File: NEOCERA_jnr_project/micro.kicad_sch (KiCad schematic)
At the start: 0 parts

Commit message: fully edited
edited :)
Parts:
- added D3: SM712_SOT23, Package_TO_SOT_SMD:SOT-23, symbol Diode:SM712_SOT23
- added D4: LED, LED_SMD:LED_0805_2012Metric, symbol Device:LED
- added FID1, FID2, FID3, FID4: Fiducial, Fiducial:Fiducial_1mm_Mask2mm, symbol Mechanical:Fiducial
- added R25: R, symbol Device:R
- added R26: 10k, symbol Device:R
- added TP1: TestPoint, TestPoint:TestPoint_THTPad_2.0x2.0mm_Drill1.0mm, symbol Connector:TestPoint
- added U12: PIC18F45K50_QFP, Package_QFP:TQFP-44_10x10mm_P0.8mm, symbol MCU_Microchip_PIC18:PIC18F45K50_QFP
- added Y1: ASV-xxxMHz, Oscillator:Oscillator_SMD_Abracon_ASV-4Pin_7.0x5.1mm, symbol Oscillator:ASV-xxxMHz
- added Y2: MAX7375AXR365, Package_TO_SOT_SMD:SOT-323_SC-70, symbol Oscillator:MAX7375AXR365
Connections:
- new net: R25.1, U12.3 (RD5/P1B/AN25)
- new net: U12.30 (OSC1/CLKI/RA7), Y1.3 (OUT)
- new net: R26.2, Y1.1 (EN)
- new net: D4.2 (A), R25.2
- new net +3.3V: R26.1, U12.28 (VDD), U12.8 (AN12/SRI/~{FLT0}/SDI/SDA/INT0/RB0), Y1.4 (Vdd)
- new net GND: D4.1 (K), TP1.1, U12.29 (VSS), U12.7 (VDD), Y1.2 (GND)

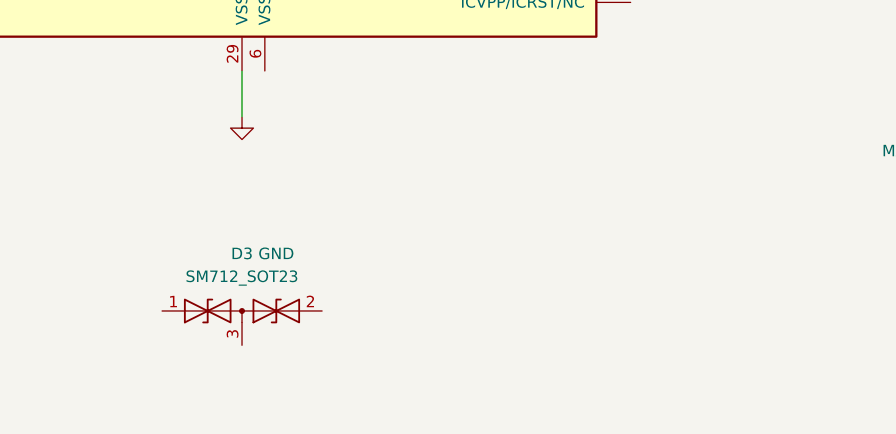
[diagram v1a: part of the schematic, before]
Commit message: update
- added symbol and programming header
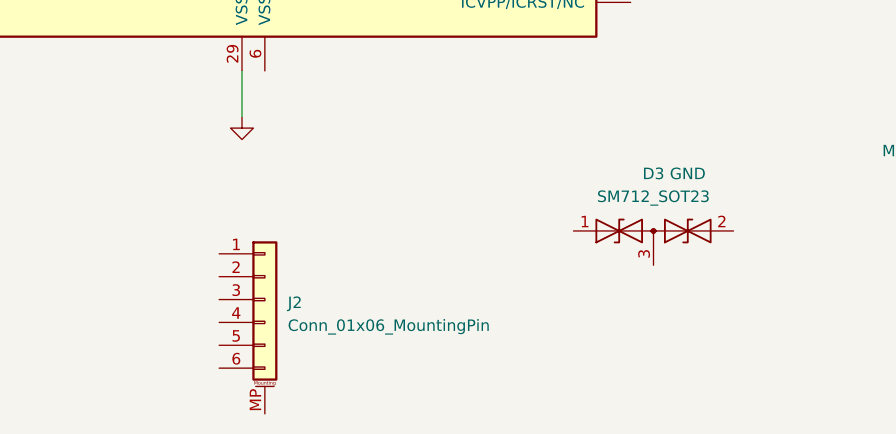
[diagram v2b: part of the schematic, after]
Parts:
- added J2: Conn_01x06_MountingPin, symbol Connector_Generic_MountingPin:Conn_01x06_MountingPin
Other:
- moved on the sheet: D3
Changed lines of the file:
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@@
+	)
+	(symbol
+		(lib_id "Connector_Generic_MountingPin:Conn_01x06_MountingPin")
+		(at 134.62 157.48 0)
+		(unit 1)
+		(exclude_from_sim no)
+		(in_bom yes)
+		(on_board yes)
+		(dnp no)
+		(fields_autoplaced yes)
+		(property "Reference" "J2"
+			(at 137.16 157.8355 0)
+			(effects
+				(font
+					(size 1.27 1.27)
+				)
+				(justify left)
+			)
+		)
+		(property "Value" "Conn_01x06_MountingPin"
+			(at 137.16 160.3755 0)
+			(effects
+				(font
+					(size 1.27 1.27)
+				)
+				(justify left)
+			)
+		)
+		(property "Footprint" ""
+			(at 134.62 157.48 0)
+			(effects
+				(font
+					(size 1.27 1.27)
+				)
+				(hide yes)
+			)
+		)
+		(property "Datasheet" "~"
+			(at 134.62 157.48 0)
+			(effects
+				(font
+					(size 1.27 1.27)
+				)
+				(hide yes)
+			)
+		)
+		(property "Description" "Generic connectable mounting pin connector, single row, 01x06, script generated (kicad-library-utils/schlib/autogen/connector/)"
+			(at 134.62 157.48 0)
+			(effects
+				(font
+					(size 1.27 1.27)
+				)
+				(hide yes)
+			)
+		)
+		(pin "5"
+		)
+		(pin "3"
+		)
+		(pin "4"
+		)
+		(pin "1"
+		)
+		(pin "6"
+		)
+		(pin "2"
+		)
+		(pin "MP"
+		)
+		(instances
+			(project ""
+				(path "/a8746ab6-0163-416c-99f9-0036ded73fc6/31b6b5cc-d086-44ba-8cec-c6130e1adfec"
+					(reference "J2")
+					(unit 1)
+				)
+			)
+		)
 	)
 	(symbol
@@
 		)
 		(property "Value" "GND"
-			(at 135.89 152.4 0)
+			(at 181.61 143.51 0)
 			(effects
 				(font
@@
 	(symbol
 		(lib_id "Diode:SM712_SOT23")
-		(at 132.08 158.75 0)
+		(at 177.8 149.86 0)
 		(unit 1)
 		(exclude_from_sim no)
@@
 		(fields_autoplaced yes)
 		(property "Reference" "D3"
-			(at 132.08 152.4 0)
+			(at 177.8 143.51 0)
 			(effects
 				(font
@@
 		)
 		(property "Value" "SM712_SOT23"
-			(at 132.08 154.94 0)
+			(at 177.8 146.05 0)
 			(effects
 				(font
@@
 		)
 		(property "Footprint" "Package_TO_SOT_SMD:SOT-23"
-			(at 132.08 167.64 0)
+			(at 177.8 158.75 0)
 			(effects
 				(font
@@
 		)
 		(property "Datasheet" "https://www.littelfuse.com/~/media/electronics/datasheets/tvs_diode_arrays/littelfuse_tvs_diode_array_sm712_datasheet.pdf.pdf"
-			(at 128.27 158.75 0)
+			(at 173.99 149.86 0)
 			(effects
 				(font
@@
 		)
 		(property "Description" "7V/12V, 600W Asymmetrical TVS Diode Array, SOT-23"
-			(at 132.08 158.75 0)
-			(effects
-				(font
+			(at 177.8 149.86 0)
+			(effects
+				(font

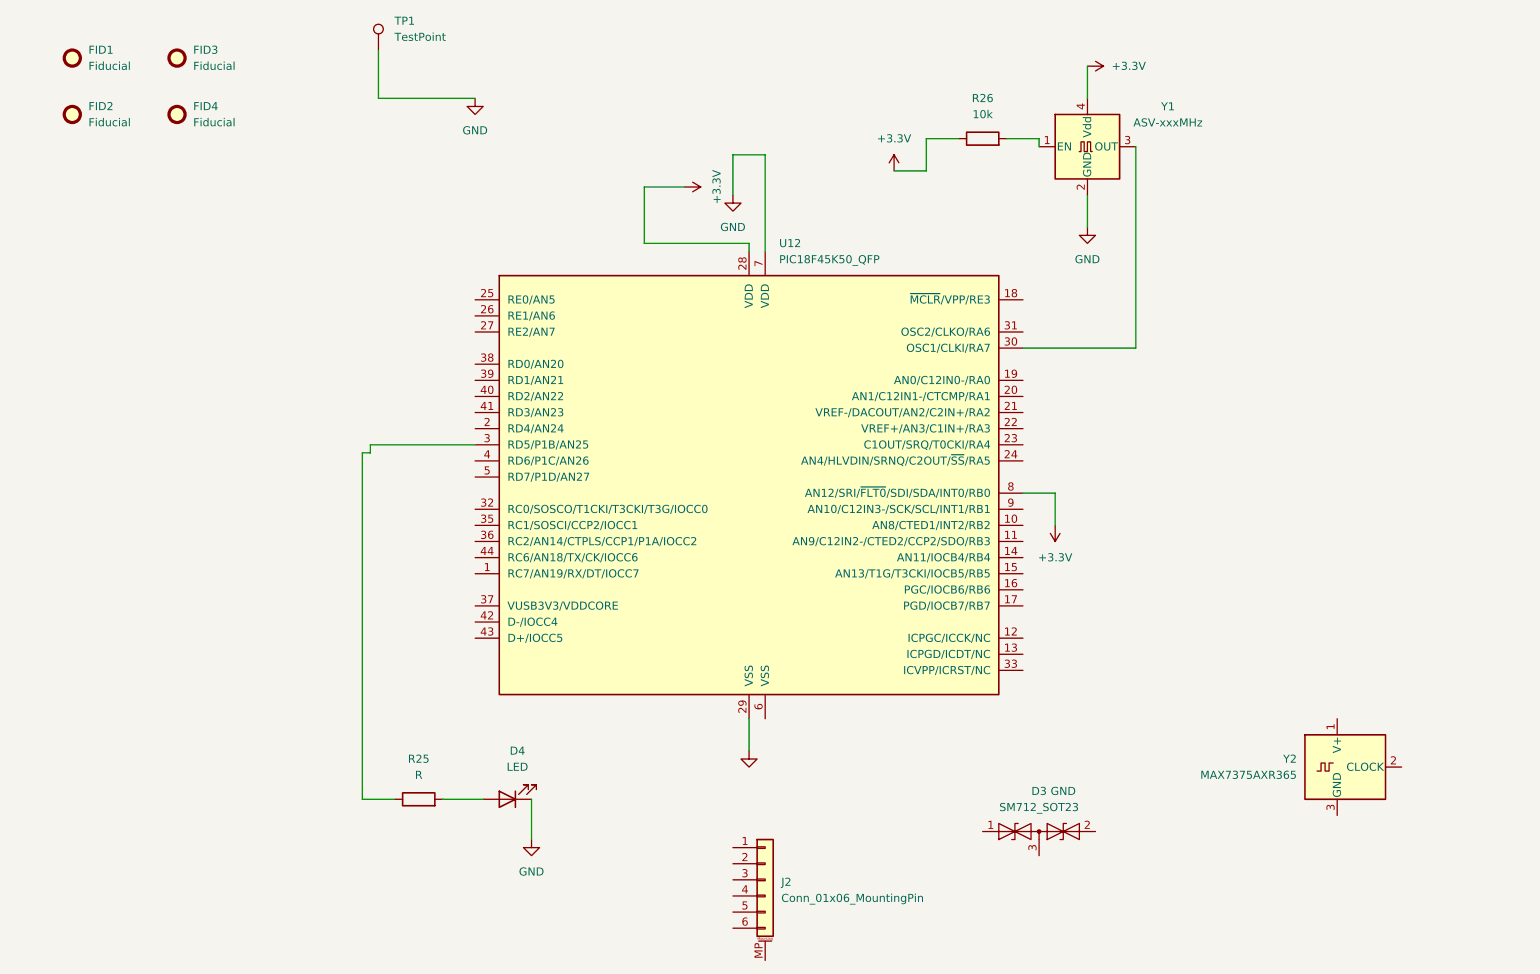
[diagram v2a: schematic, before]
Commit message: Complete micro design
Added footprints, and missing symbols
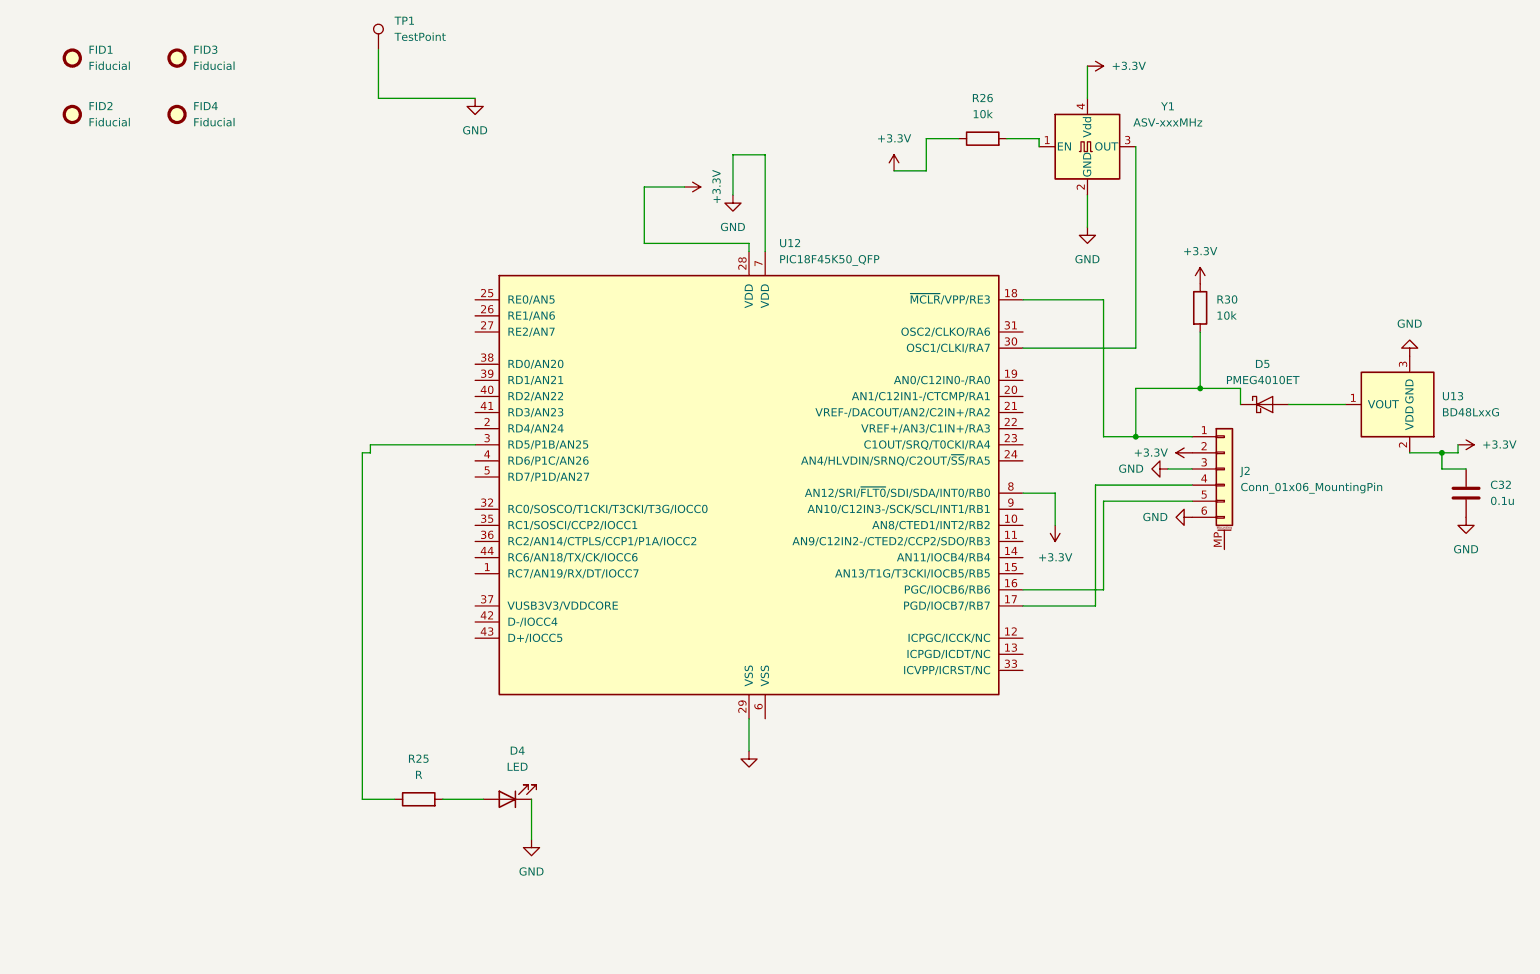
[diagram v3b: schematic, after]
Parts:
- removed D3: SM712_SOT23, Package_TO_SOT_SMD:SOT-23, symbol Diode:SM712_SOT23
- removed Y2: MAX7375AXR365, Package_TO_SOT_SMD:SOT-323_SC-70, symbol Oscillator:MAX7375AXR365
- added C32: 0.1u, Capacitor_SMD:C_0201_0603Metric, symbol Device:C
- added D5: PMEG4010ET, Package_TO_SOT_SMD:SOT-23, symbol Diode:PMEG4010ET
- added R30: 10k, Resistor_SMD:R_0201_0603Metric, symbol Device:R
- added U13: BD48LxxG, Package_TO_SOT_SMD:SOT-23, symbol Power_Management:BD48LxxG
- J2: footprint (none) -> MountingHole:MountingHole_2.1mm
- R25, R26: footprint (none) -> Resistor_SMD:R_0201_0603Metric
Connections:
- net +3.3V: now also J2.2 (Pin_2), C32.1, R30.1, U13.2 (VDD)
- net GND: now also J2.3 (Pin_3), J2.6 (Pin_6), C32.2, U13.3 (GND)
- net at U12.16 (PGC/IOCB6/RB6): now also J2.5 (Pin_5)
- net at U12.17 (PGD/IOCB7/RB7): now also J2.4 (Pin_4)
- net at U12.18 (~{MCLR}/VPP/RE3): now also J2.1 (Pin_1), D5.3 (K), R30.2
- new net: D5.1 (A), U13.1 (VOUT)

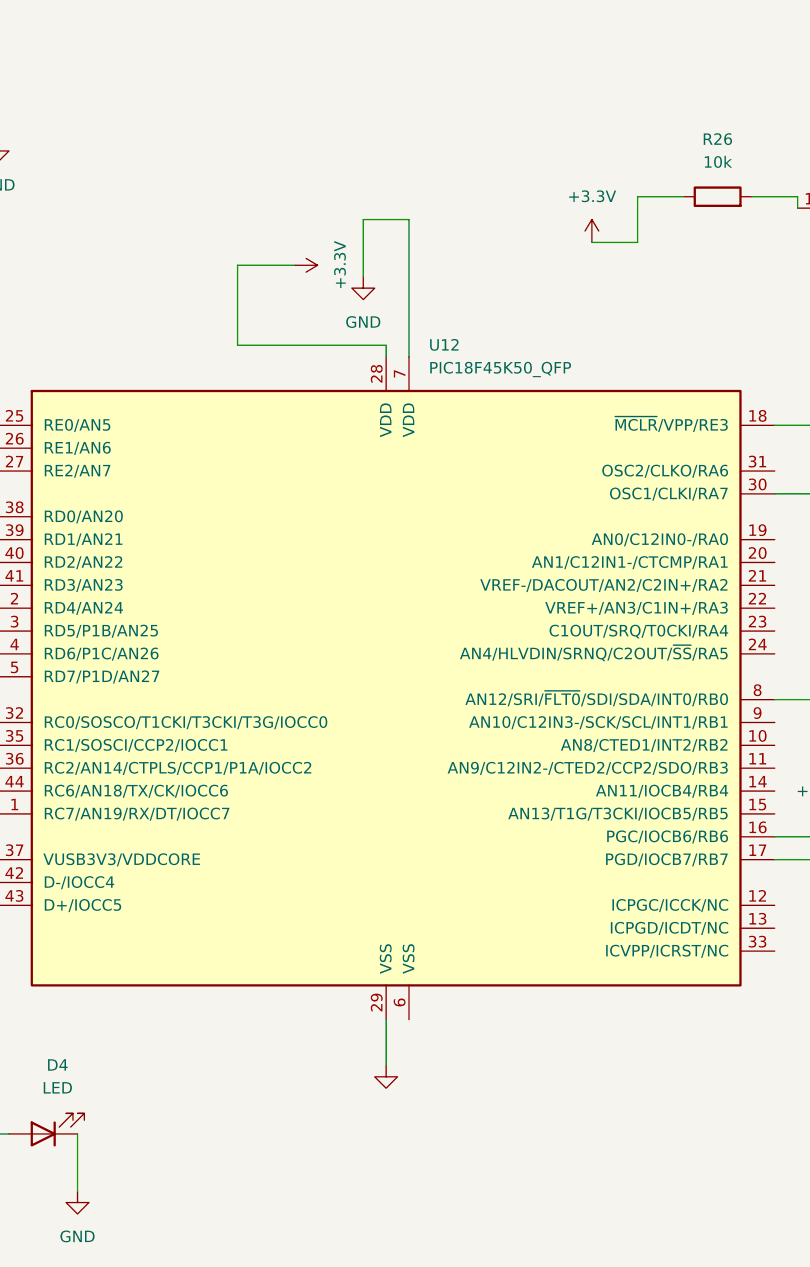
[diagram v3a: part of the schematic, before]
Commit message: updated micro design
added a capacitor after project report
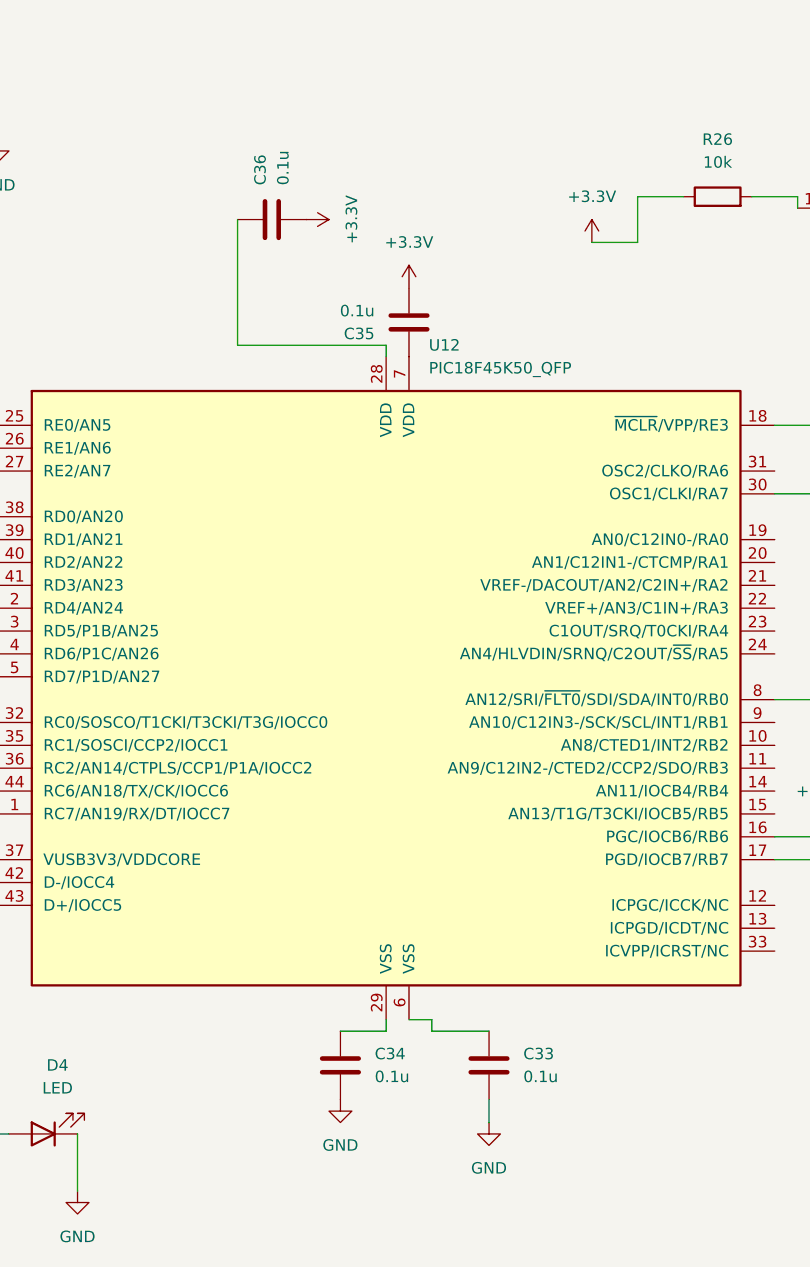
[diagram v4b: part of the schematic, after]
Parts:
- added C33, C34, C35, C36: 0.1u, Capacitor_SMD:C_0201_0603Metric, symbol Device:C
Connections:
- net +3.3V: now also C35.2, C36.2; no longer U12.28 (VDD)
- net GND: now also C33.2, C34.2; no longer U12.29 (VSS), U12.7 (VDD)
- net at U12.6 (VSS): now also C33.1
- new net: C36.1, U12.28 (VDD)
- new net: C34.1, U12.29 (VSS)
- new net: C35.1, U12.7 (VDD)

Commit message: changes
edited symbols and usb schematic
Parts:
- C32, C33, C34, C35, C36: footprint Capacitor_SMD:C_0201_0603Metric -> Capacitor_SMD:C_0603_1608Metric_Pad1.08x0.95mm_HandSolder
- R25, R26, R30: footprint Resistor_SMD:R_0201_0603Metric -> Resistor_SMD:R_0603_1608Metric_Pad0.98x0.95mm_HandSolder
- TP1: footprint TestPoint:TestPoint_THTPad_2.0x2.0mm_Drill1.0mm -> TestPoint:TestPoint_THTPad_D3.0mm_Drill1.5mm
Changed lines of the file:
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@@
 			)
 		)
-		(property "Footprint" "Resistor_SMD:R_0201_0603Metric"
+		(property "Footprint" "Resistor_SMD:R_0603_1608Metric_Pad0.98x0.95mm_HandSolder"
 			(at 201.422 67.31 90)
 			(effects
@@
 			)
 		)
-		(property "Footprint" "TestPoint:TestPoint_THTPad_2.0x2.0mm_Drill1.0mm"
+		(property "Footprint" "TestPoint:TestPoint_THTPad_D3.0mm_Drill1.5mm"
 			(at 78.74 26.67 0)
 			(effects
@@
 			)
 		)
-		(property "Footprint" "Capacitor_SMD:C_0201_0603Metric"
+		(property "Footprint" "Capacitor_SMD:C_0603_1608Metric_Pad1.08x0.95mm_HandSolder"
 			(at 133.6548 50.8 0)
 			(effects
@@
 			)
 		)
-		(property "Footprint" "Capacitor_SMD:C_0201_0603Metric"
+		(property "Footprint" "Capacitor_SMD:C_0603_1608Metric_Pad1.08x0.95mm_HandSolder"
 			(at 246.0752 100.33 0)
 			(effects
@@
 			)
 		)
-		(property "Footprint" "Capacitor_SMD:C_0201_0603Metric"
+		(property "Footprint" "Capacitor_SMD:C_0603_1608Metric_Pad1.08x0.95mm_HandSolder"
 			(at 127.9652 140.97 0)
 			(effects
@@
 			)
 		)
-		(property "Footprint" "Capacitor_SMD:C_0201_0603Metric"
+		(property "Footprint" "Capacitor_SMD:C_0603_1608Metric_Pad1.08x0.95mm_HandSolder"
 			(at 144.4752 140.97 0)
 			(effects
@@
 			)
 		)
-		(property "Footprint" "Resistor_SMD:R_0201_0603Metric"
+		(property "Footprint" "Resistor_SMD:R_0603_1608Metric_Pad0.98x0.95mm_HandSolder"
 			(at 80.01 146.558 90)
 			(effects
@@
 			)
 		)
-		(property "Footprint" "Capacitor_SMD:C_0201_0603Metric"
+		(property "Footprint" "Capacitor_SMD:C_0603_1608Metric_Pad1.08x0.95mm_HandSolder"
 			(at 123.19 42.2148 0)
 			(effects
@@
 			)
 		)
-		(property "Footprint" "Resistor_SMD:R_0201_0603Metric"
+		(property "Footprint" "Resistor_SMD:R_0603_1608Metric_Pad0.98x0.95mm_HandSolder"
 			(at 168.91 42.418 90)
 			(effects

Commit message: bunch
bunch
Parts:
- removed D4: LED, LED_SMD:LED_0805_2012Metric, symbol Device:LED
- added D3: LED, LED_SMD:LED_0805_2012Metric, symbol Device:LED
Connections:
- net GND: now also D3.1 (K)
- net at R25.2: now also D3.2 (A)

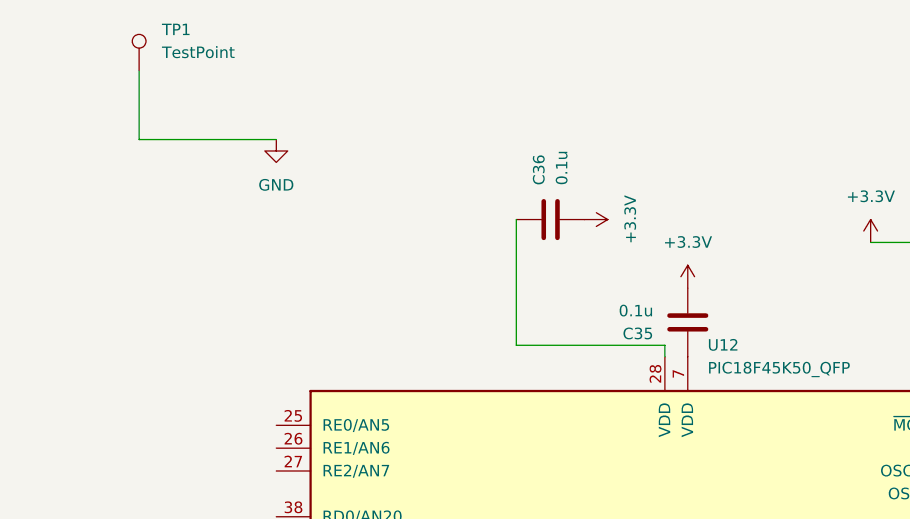
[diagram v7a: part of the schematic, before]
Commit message: symbols changed
edited all symbols
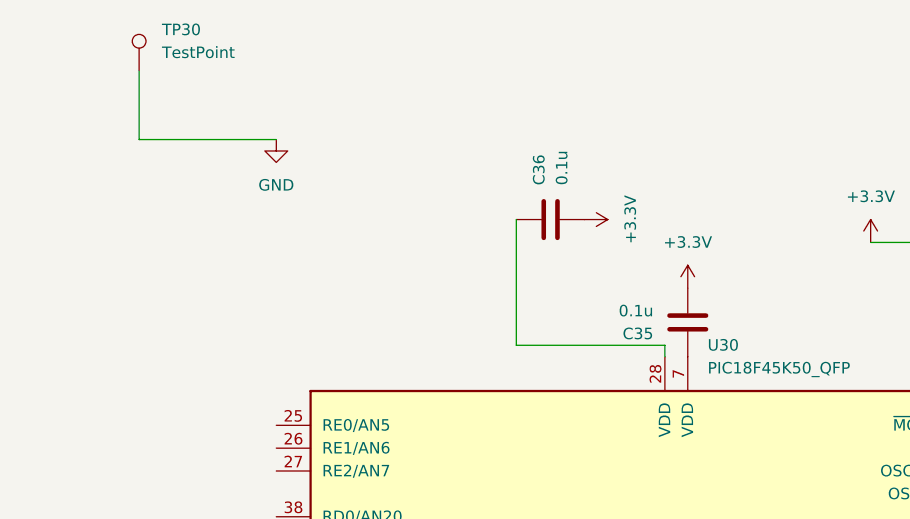
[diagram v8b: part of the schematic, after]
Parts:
- renumbered TP1 to TP30, U12 to U30
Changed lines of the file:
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@@
 		(dnp no)
 		(fields_autoplaced yes)
-		(property "Reference" "U12"
+		(property "Reference" "U30"
 			(at 136.8141 57.15 0)
 			(effects
@@
 			(project ""
 				(path "/a8746ab6-0163-416c-99f9-0036ded73fc6/31b6b5cc-d086-44ba-8cec-c6130e1adfec"
-					(reference "U12")
+					(reference "U30")
 					(unit 1)
 				)
@@
 		(dnp no)
 		(fields_autoplaced yes)
-		(property "Reference" "TP1"
+		(property "Reference" "TP30"
 			(at 76.2 22.0979 0)
 			(effects
@@
 			(project ""
 				(path "/a8746ab6-0163-416c-99f9-0036ded73fc6/31b6b5cc-d086-44ba-8cec-c6130e1adfec"
-					(reference "TP1")
-					(unit 1)
-				)
+					(reference "TP30")
+					(unit 1)
+				)
